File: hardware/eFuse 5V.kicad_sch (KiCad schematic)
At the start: 7 parts, among them IC4 NIS6351MT2TXG

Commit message: changed some footprints for clarity, and made some progress on board
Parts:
- added D10, D9: D_SCH, Diode_SMD:D_0603_1608Metric, symbol Device:D_Schottky_Small
- added O4: FOD8802DR2_IMG, FOD8802DR2:SOIC127P600X175-8N, symbol FOD8802DR2:FOD8802DR2_IMG
- added R17, R18, R41, R42, R53: 10k, Resistor_SMD:R_0603_1608Metric, symbol Device:R_Small
- C39: value C? -> 100nF
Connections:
- net FLAG: now also O4.7, R42.2; no longer IC4.6 (FLAG)
- net GND: now also D10.2 (A), D9.2 (A), O4.2, O4.4, R42.1, R53.1
- net ~{EN}: now also R18.2; no longer IC4.7 (EN)
- new net: O4.8, R41.1
- new net: D9.1 (K), O4.1, R17.1
- new net: D10.1 (K), O4.3, R18.1
- new net: O4.5, R53.2
- new net +3V3: R41.2
- new net WATER/POT_EN: IC4.7 (EN), O4.6
- new net WATER/POT_FLAG: IC4.6 (FLAG), R17.2
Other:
- moved on the sheet: C39, CLAMP1, F2, ILIM3, ILIM4, R44

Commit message: finished new wersion of the board
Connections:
- net ~{EN} renamed ~{ENABLE}
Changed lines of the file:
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@@
     (effects (font (size 1.27 1.27)) (justify right))
   )
-  (hierarchical_label "~{EN}" (shape input) (at 193.04 93.345 180)
+  (hierarchical_label "~{ENABLE}" (shape input) (at 193.04 93.345 180)
     (effects (font (size 1.27 1.27)) (justify right))
   )

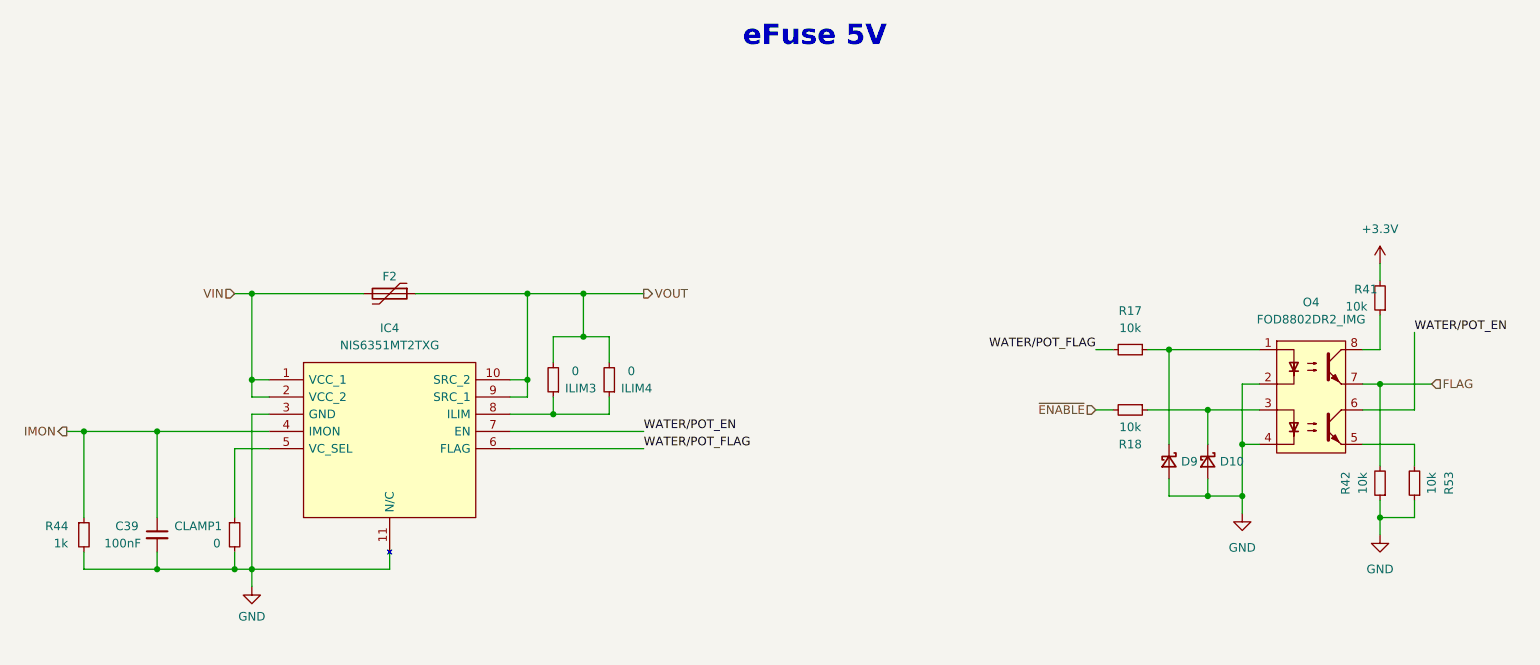
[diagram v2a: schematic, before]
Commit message: debuged the board, changed one opto for mosfet, changed the way water and potentiometers were supplied. Also standrised opamps (yoinked opamps from data Data_Acquisition_Cards)
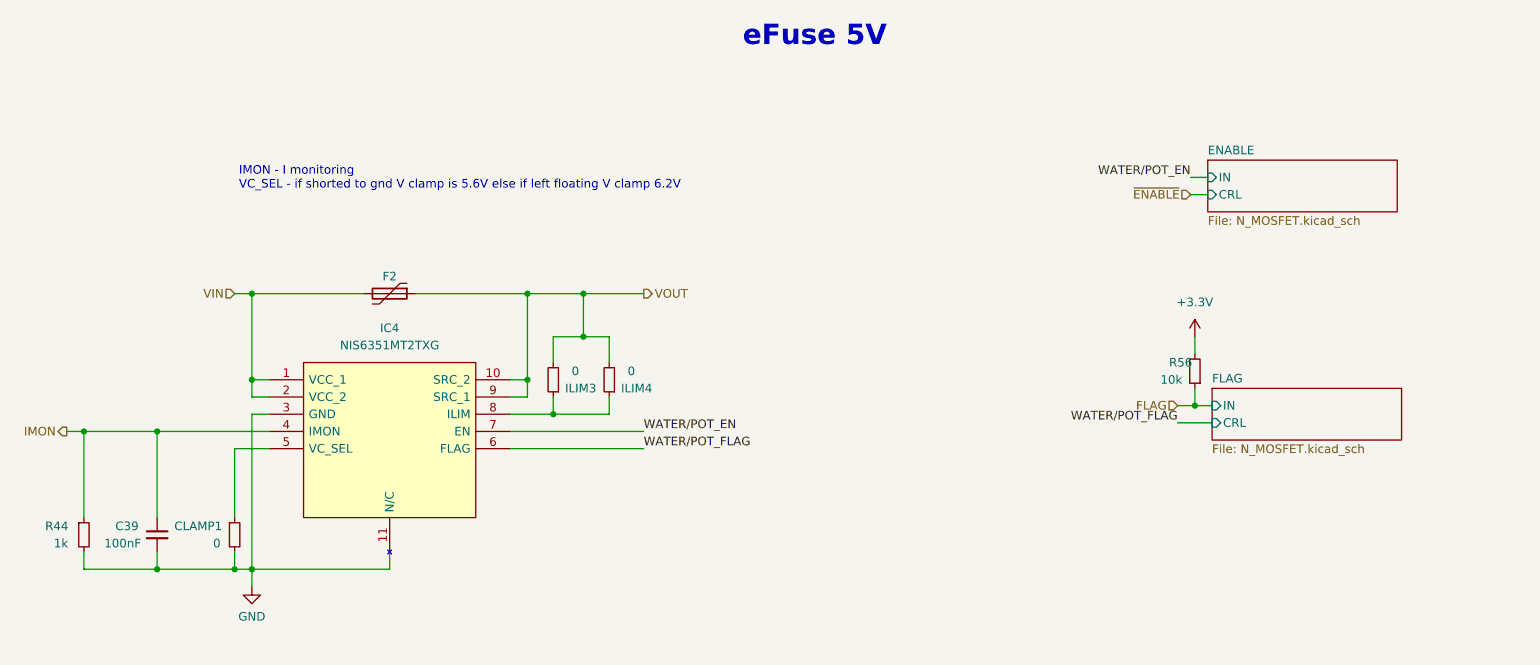
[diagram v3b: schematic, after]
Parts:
- removed D10, D9: D_SCH, Diode_SMD:D_0603_1608Metric, symbol Device:D_Schottky_Small
- removed O4: FOD8802DR2_IMG, FOD8802DR2:SOIC127P600X175-8N, symbol FOD8802DR2:FOD8802DR2_IMG
- removed R17, R18, R41, R42, R53: 10k, Resistor_SMD:R_0603_1608Metric, symbol Device:R_Small
- added R56: 10k, Resistor_SMD:R_0603_1608Metric, symbol Device:R_Small
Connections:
- net +3V3: now also R56.2
- net FLAG: now also R56.1
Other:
- added sheet ENABLE (N_MOSFET.kicad_sch)
- added sheet FLAG (N_MOSFET.kicad_sch)
- note added: "IMON - I monitoring VC_SEL - if shorted to gnd V clamp is 5.6V else if left floating V clamp 6.2V"
